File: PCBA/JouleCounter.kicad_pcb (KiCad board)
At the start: 2 copper layers, 5 x 8.2 mm, 31 parts, among them J501 USB_C_Receptacle, J502 USB_C_Receptacle_USB2.0, J601 USB_C_Receptacle_USB2.0, SW801 SW_Push, SW802 SW_Push, SW803 SW_Push, SW804 SW_Push, U201 BL604, U401 FUSB302B, U601 CH340E, U701 INA181

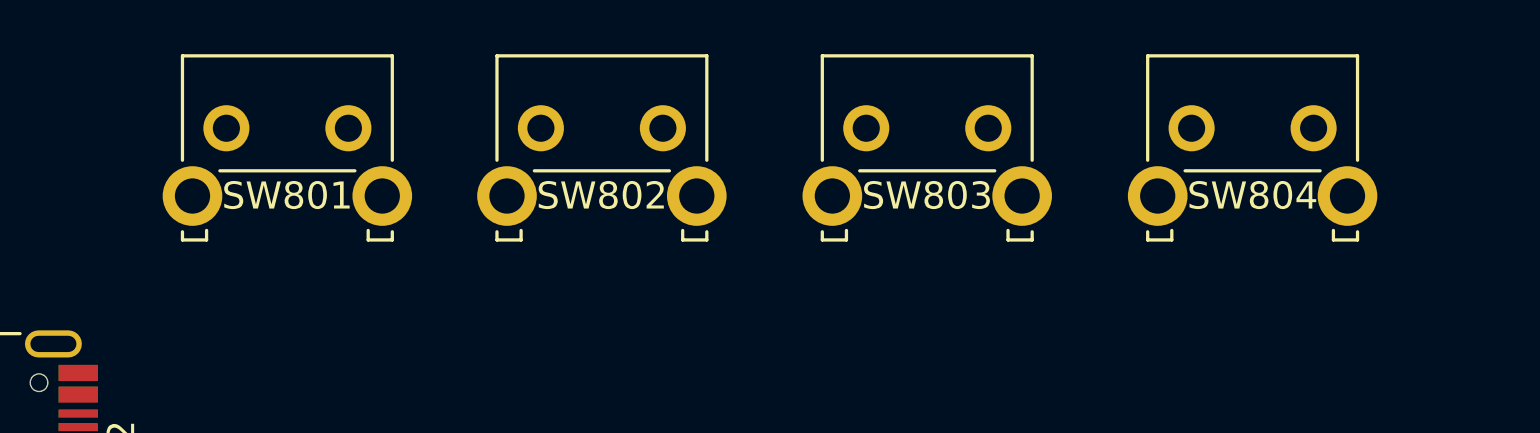
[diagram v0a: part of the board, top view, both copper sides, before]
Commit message: Assign footprints
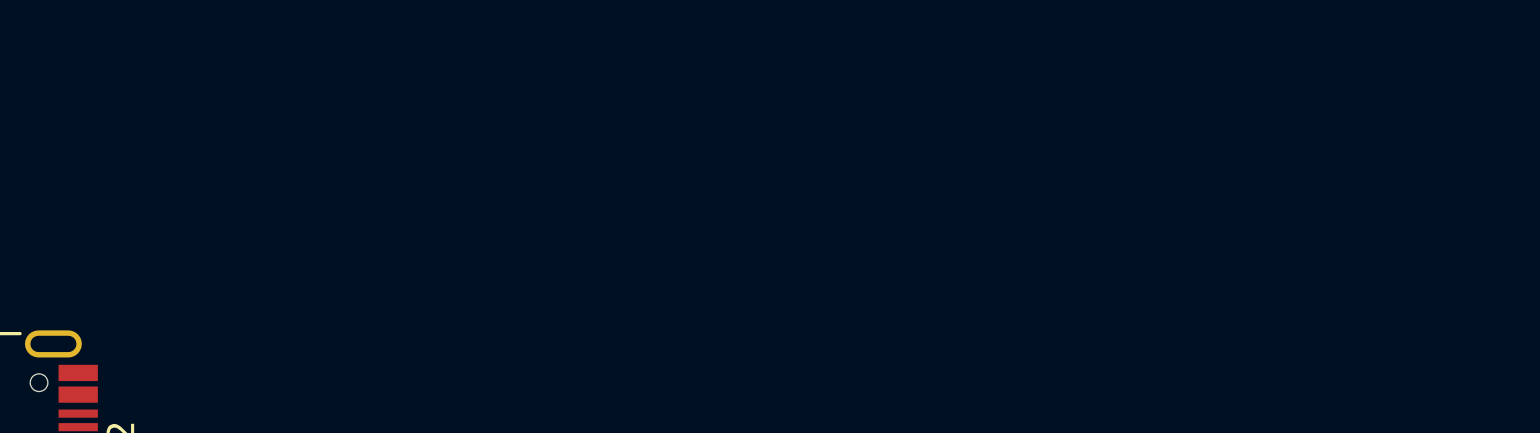
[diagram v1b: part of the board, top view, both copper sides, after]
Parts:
- removed SW801, SW802, SW803, SW804: SW_Push, Button_Switch_THT:SW_Tactile_SKHH_Angled

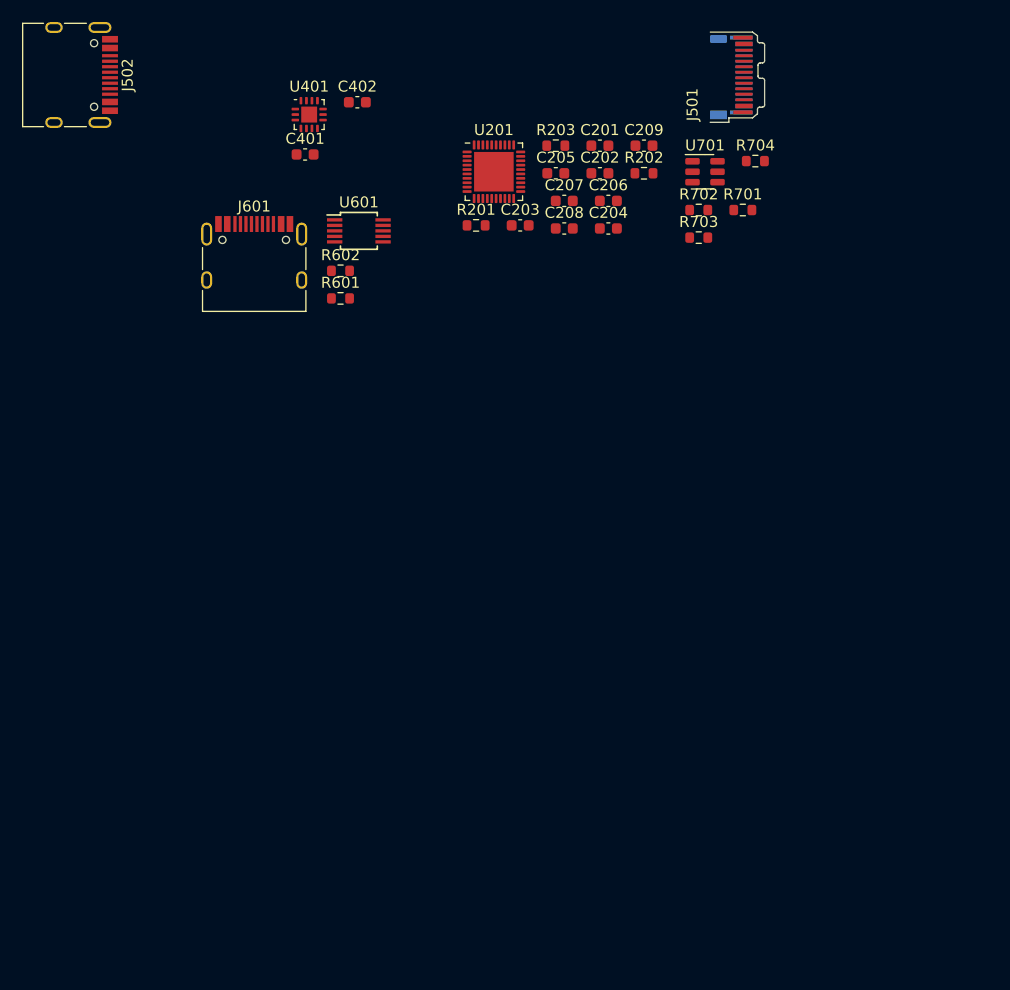
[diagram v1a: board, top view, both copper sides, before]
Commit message: Update schematic pinmap bl706
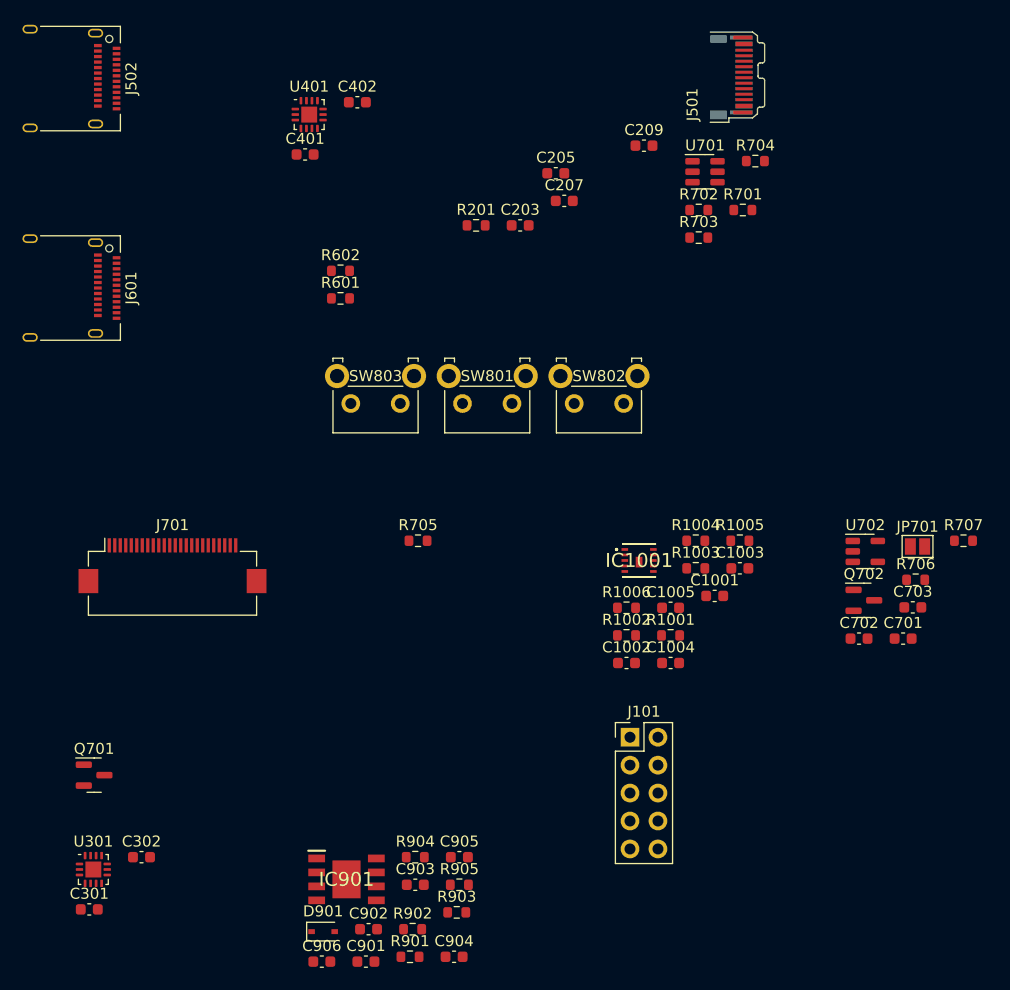
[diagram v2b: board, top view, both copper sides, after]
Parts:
- removed C201, C204: 0.1uF, Capacitor_SMD:C_0603_1608Metric
- removed C202, C206, C208: 1uF, Capacitor_SMD:C_0603_1608Metric
- removed R202, R203: 10k, Resistor_SMD:R_0603_1608Metric
- removed U201: BL604, Package_DFN_QFN:QFN-40-1EP_5x5mm_P0.4mm_EP3.6x3.6mm
- removed U601: CH340E, Package_SO:MSOP-10_3x3mm_P0.5mm
- added C1001: 100nF, Capacitor_SMD:C_0603_1608Metric, F.Cu at (158.5, 107.4)
- added C1002: 2.2uF, Capacitor_SMD:C_0603_1608Metric, F.Cu at (150.5, 113.5)
- added C1003: 2.2uF, Capacitor_SMD:C_0603_1608Metric, F.Cu at (160.8, 104.9)
- added C1004: 2.2uF, Capacitor_SMD:C_0603_1608Metric, F.Cu at (154.5, 113.5)
- added C1005: C, Capacitor_SMD:C_0603_1608Metric, F.Cu at (154.5, 108.5)
- added C301: 1uF, Capacitor_SMD:C_0603_1608Metric, F.Cu at (101.6, 135.9)
- added C302: 1uF, Capacitor_SMD:C_0603_1608Metric, F.Cu at (106.3, 131.1)
- added C701: C, Capacitor_SMD:C_0603_1608Metric, F.Cu at (175.6, 111.3)
- added C702: C, Capacitor_SMD:C_0603_1608Metric, F.Cu at (171.6, 111.3)
- added C703: C, Capacitor_SMD:C_0603_1608Metric, F.Cu at (176.5, 108.4)
- added C901: 47uF, Capacitor_SMD:C_0603_1608Metric, F.Cu at (126.8, 140.6)
- added C902: 4.7uF, Capacitor_SMD:C_0603_1608Metric, F.Cu at (127.0, 137.7)
- added C903: -, Capacitor_SMD:C_0603_1608Metric, F.Cu at (131.2, 133.7)
- added C904: -, Capacitor_SMD:C_0603_1608Metric, F.Cu at (134.8, 140.2)
- added C905: 100nF, Capacitor_SMD:C_0603_1608Metric, F.Cu at (135.3, 131.1)
- added C906: 4.7uF, Capacitor_SMD:C_0603_1608Metric, F.Cu at (122.8, 140.6)
- added D901: D_Schottky, Diode_SMD:D_SOD-323, F.Cu at (122.9, 137.9)
- added IC1001: L7983PU33R, L7983PU33R:L7983PU33R, F.Cu at (151.6, 104.2)
- added IC901: MP4560DN-LF-Z, MP4560DN:SOIC127P600X170-9N, F.Cu at (125.0, 133.2)
- added J101: JTAG, Connector_PinHeader_2.54mm:PinHeader_2x05_P2.54mm_Vertical, F.Cu at (150.8, 120.2)
- added J701: FH12-24S-0.5SH(55), Connector_FFC-FPC:Hirose_FH12-24S-0.5SH_1x24-1MP_P0.50mm_Horizontal, F.Cu at (109.2, 104.6)
- added JP701: Disable, Jumper:SolderJumper-2_P1.3mm_Open_Pad1.0x1.5mm, F.Cu at (176.9, 102.9)
- added Q701: 2N7002, Package_TO_SOT_SMD:SOT-23, F.Cu at (102.0, 123.7)
- added Q702: MMBT3904, Package_TO_SOT_SMD:SOT-23, F.Cu at (172.1, 107.8)
- added R1001: 0, Resistor_SMD:R_0603_1608Metric, F.Cu at (154.5, 111.0)
- added R1002: DNP, Resistor_SMD:R_0603_1608Metric, F.Cu at (150.5, 111.0)
- added R1003: 0, Resistor_SMD:R_0603_1608Metric, F.Cu at (156.8, 104.9)
- added R1004: 100k, Resistor_SMD:R_0603_1608Metric, F.Cu at (156.8, 102.4)
- added R1005: 180k, Resistor_SMD:R_0603_1608Metric, F.Cu at (160.8, 102.4)
- added R1006: 68k, Resistor_SMD:R_0603_1608Metric, F.Cu at (150.5, 108.5)
- added R705: 200?, Resistor_SMD:R_0603_1608Metric, F.Cu at (131.5, 102.4)
- added R706: 100k, Resistor_SMD:R_0603_1608Metric, F.Cu at (176.8, 105.9)
- added R707: 1M, Resistor_SMD:R_0603_1608Metric, F.Cu at (181.1, 102.4)
- added R901: 200k, Resistor_SMD:R_0603_1608Metric, F.Cu at (130.8, 140.2)
- added R902: -, Resistor_SMD:R_0603_1608Metric, F.Cu at (131.0, 137.7)
- added R903: -, Resistor_SMD:R_0603_1608Metric, F.Cu at (135.0, 136.2)
- added R904: 200k, Resistor_SMD:R_0603_1608Metric, F.Cu at (131.2, 131.1)
- added R905: 200k, Resistor_SMD:R_0603_1608Metric, F.Cu at (135.3, 133.7)
- added SW801: SW_Push, Button_Switch_THT:SW_Tactile_SKHH_Angled, F.Cu at (140.0, 89.9)
- added SW802: SW_Push, Button_Switch_THT:SW_Tactile_SKHH_Angled, F.Cu at (150.2, 89.9)
- added SW803: SW_Push, Button_Switch_THT:SW_Tactile_SKHH_Angled, F.Cu at (129.9, 89.9)
- added U301: FUSB302B, Package_DFN_QFN:WQFN-14-1EP_2.5x2.5mm_P0.5mm_EP1.45x1.45mm, F.Cu at (102.0, 132.3)
- added U702: TC2014-3.3VxCTTR, Package_TO_SOT_SMD:SOT-23-5, F.Cu at (172.2, 103.3)
- J502, J601: value USB_C_Receptacle_USB2.0 -> USB_C_Receptacle; footprint Connector_USB:USB_C_Receptacle_HRO_TYPE-C-31-M-12 -> Connector_USB:USB_C_Receptacle_Amphenol_12401610E4-2A
- moved J601 17.6 mm to (99.1, 79.4), turned to -90 degrees
- moved J502 0.50 mm to (99.1, 60.3)
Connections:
- net /Programming/5V renamed /5V_USB
- net /~{FUSB IRQ} renamed /~{FUSB IRQ0}
- net AVDD33 renamed VDD
- net Net-(J601-PadA6) renamed /USB D+
- net Net-(J601-PadA7) renamed /USB D-
- J501 pad A10: unconnected-(J501-PadA10) -> Net-(J501-PadA10)
- J501 pad A11: unconnected-(J501-PadA11) -> Net-(J501-PadA11)
- J501 pad A2: unconnected-(J501-PadA2) -> Net-(J501-PadA2)
- J501 pad A3: unconnected-(J501-PadA3) -> Net-(J501-PadA3)
- J501 pad B10: unconnected-(J501-PadB10) -> Net-(J501-PadB10)
- J501 pad B11: unconnected-(J501-PadB11) -> Net-(J501-PadB11)
- J501 pad B2: unconnected-(J501-PadB2) -> Net-(J501-PadB2)
- J501 pad B3: unconnected-(J501-PadB3) -> Net-(J501-PadB3)
- J502 pad A5: /CC1 -> /CC1_X
- J502 pad B5: /CC2 -> /CC2_X
- J601 pad A8: unconnected-(J601-PadA8) -> /Uart Tx
- J601 pad B8: unconnected-(J601-PadB8) -> /Uart Rx
- R201 pad 1: /BootMode -> unconnected-(R201-Pad1)

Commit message: Rough outline
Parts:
- removed J701: FH12-24S-0.5SH(55), Connector_FFC-FPC:Hirose_FH12-24S-0.5SH_1x24-1MP_P0.50mm_Horizontal
- removed R705: 200?, Resistor_SMD:R_0603_1608Metric
- added AE201: KH2012F245C04, Resistor_SMD:R_0805_2012Metric, F.Cu at (231.4, 123.0)
- added C201: 1uF, Capacitor_SMD:C_0603_1608Metric, F.Cu at (252.8, 116.6)
- added C202: 1uF, Capacitor_SMD:C_0603_1608Metric, F.Cu at (247.8, 119.2)
- added C204: 1uF, Capacitor_SMD:C_0603_1608Metric, F.Cu at (243.5, 122.4)
- added C206: 100nF, Capacitor_SMD:C_0603_1608Metric, F.Cu at (247.8, 121.7)
- added C208: 1uF, Capacitor_SMD:C_0603_1608Metric, F.Cu at (252.8, 114.1)
- added C210: 100nF, Capacitor_SMD:C_0603_1608Metric, F.Cu at (256.8, 114.1)
- added C211: -, Capacitor_SMD:C_0603_1608Metric, F.Cu at (251.8, 119.2)
- added C212: -, Capacitor_SMD:C_0603_1608Metric, F.Cu at (247.5, 124.2)
- added C213: 0.1uF, Capacitor_SMD:C_0603_1608Metric, F.Cu at (256.4, 117.8)
- added C907: C, Capacitor_SMD:C_0603_1608Metric, F.Cu at (178.6, 55.4)
- added C908: 0.1u, Capacitor_SMD:C_0603_1608Metric, F.Cu at (178.6, 60.4)
- added C909: 0.1u, Capacitor_SMD:C_0603_1608Metric, F.Cu at (178.6, 57.9)
- added C910: 0.1u, Capacitor_SMD:C_0603_1608Metric, F.Cu at (182.6, 57.9)
- added C911: 1uf, Capacitor_SMD:C_0603_1608Metric, F.Cu at (182.6, 55.4)
- added J901: Conn_02x25_Odd_Even_MountingPin, Connector_FFC-FPC:Molex_54132-5033_1x50-1MP_P0.5mm_Horizontal, F.Cu at (215.4, 81.9)
- added L1001: 47uH, Inductor_SMD:L_Taiyo-Yuden_NR-40xx_HandSoldering, F.Cu at (179.8, 21.2)
- added L201: 2.2uH, Inductor_SMD:L_Wuerth_MAPI-3010, F.Cu at (248.3, 115.4)
- added L901: 15, Inductor_SMD:L_Wuerth_MAPI-3010, F.Cu at (162.2, 35.2)
- added R202: 0, Resistor_SMD:R_0603_1608Metric, F.Cu at (239.5, 122.4)
- added R501: 0.02, Resistor_SMD:R_Shunt_Vishay_WSK2512_6332Metric_T1.19mm, F.Cu at (230.5, 92.1)
- added R906: 200?, Resistor_SMD:R_0603_1608Metric, F.Cu at (183.5, 46.5)
- added R907: 200?, Resistor_SMD:R_0603_1608Metric, F.Cu at (178.4, 50.9)
- added R908: 200?, Resistor_SMD:R_0603_1608Metric, F.Cu at (186.4, 49.0)
- added R909: 200?, Resistor_SMD:R_0603_1608Metric, F.Cu at (182.4, 50.9)
- added SW501: SW_DIP_x02, Button_Switch_SMD:SW_DIP_SPSTx02_Slide_Copal_CHS-02A_W5.08mm_P1.27mm_JPin, B.Cu at (230.4, 67.8)
- added U201: BL706, Package_DFN_QFN:QFN-48-1EP_6x6mm_P0.4mm_EP4.2x4.2mm, F.Cu at (213.0, 94.3)
- added U901: LP2985-2.8, Package_TO_SOT_SMD:SOT-23-5, F.Cu at (178.9, 47.5)
- added Y201: 40MHz, Crystal:Crystal_SMD_2016-4Pin_2.0x1.6mm, F.Cu at (251.7, 122.2)
- moved J502 138.8 mm to (230.5, 104.8), turned to 0 degrees
- moved Q701 134.1 mm to (213.2, 48.6)
- moved C203 129.1 mm to (257.4, 129.1)
- moved C205 129.1 mm to (260.6, 124.4)
- moved C207 129.1 mm to (261.4, 126.9)
- moved C209 129.1 mm to (268.6, 121.9)
- moved R201 129.1 mm to (253.3, 129.1)
- moved C301 125.6 mm to (222.5, 101.8)
- moved U301 123.7 mm to (222.5, 104.5), turned to -90 degrees
- moved C302 118.6 mm to (222.5, 107.2), turned to 180 degrees
- moved C903 114.7 mm to (162.5, 23.3)
- moved R905 114.7 mm to (166.5, 23.3)
- moved C902 114.7 mm to (158.2, 27.3)
- moved R902 114.7 mm to (162.2, 27.3)
- moved C901 114.7 mm to (158.0, 30.3)
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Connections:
- net /USB D+ DAC/ADC renamed /SENSE_USB_D+
- net /USB D- DAC/ADC renamed /SENSE_USB_D-
- net Net-(J501-PadA10) renamed /Measurement ports/RX2_-
- net Net-(J501-PadA11) renamed /Measurement ports/RX2_+
- net Net-(J501-PadA2) renamed /Measurement ports/TX1_+
- net Net-(J501-PadA3) renamed /Measurement ports/TX1_-
- net Net-(J501-PadA4) renamed /Measurement ports/VBUS2
- net Net-(J501-PadA8) renamed /Measurement ports/SBU1
- net Net-(J501-PadB10) renamed /Measurement ports/RX1_-
- net Net-(J501-PadB11) renamed /Measurement ports/RX1_+
- net Net-(J501-PadB2) renamed /Measurement ports/TX2_+
- net Net-(J501-PadB3) renamed /Measurement ports/TX2_-
- net Net-(J501-PadB8) renamed /Measurement ports/SBU2
- Q701 pad 3: Net-(J701-Pad2) -> /UI/LEDK
- R201 pad 1: unconnected-(R201-Pad1) -> /~{Reset}
- R201 pad 2: GND -> VDD
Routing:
- net /Measurement ports/RX1_+: track 0.00 -> 48.5 mm, vias 0 -> 1
- net /Measurement ports/RX1_-: track 0.00 -> 48.5 mm, vias 0 -> 1
- net /Measurement ports/TX2_-: track 0.00 -> 47.1 mm, vias 0 -> 1
- net /Measurement ports/TX2_+: track 0.00 -> 47.1 mm, vias 0 -> 1
- net /Measurement ports/TX1_+: track 0.00 -> 43.6 mm
- net /Measurement ports/TX1_-: track 0.00 -> 43.6 mm
- net /SENSE_USB_D-: track 0.00 -> 43.6 mm
- net /SENSE_USB_D+: track 0.00 -> 43.6 mm
- net /Measurement ports/RX2_+: track 0.00 -> 41.9 mm
- net /Measurement ports/RX2_-: track 0.00 -> 41.9 mm
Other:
- board size 5 x 8.2 mm -> 42 x 49 mm
- copper layers 2 -> 4

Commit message: More rough placement
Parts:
- L201: footprint Inductor_SMD:L_Wuerth_MAPI-3010 -> Inductor_SMD:L_0805_2012Metric
- moved C209 66.8 mm to (210.2, 89.5)
- moved U702 60.1 mm to (207.5, 104.5), turned to 90 degrees
- moved C205 57.2 mm to (215.5, 89.2)
- moved C201 51.7 mm to (206.0, 94.8), turned to 180 degrees
- moved C213 50.4 mm to (209.0, 100.8), turned to 180 degrees
- moved C202 47.6 mm to (206.0, 96.2), turned to 180 degrees
- moved Y201 45.2 mm to (219.5, 90.5)
- moved C203 44.5 mm to (213.0, 125.0)
- moved C207 44.5 mm to (217.0, 122.8)
- moved R201 44.5 mm to (209.0, 125.0)
- moved C211 43.1 mm to (211.8, 103.0), turned to 180 degrees
- moved L201 42.5 mm to (209.0, 99.0)
- moved C212 40.6 mm to (211.8, 104.8), turned to 180 degrees
- moved C210 40.4 mm to (221.2, 95.0)
- moved C701 38.6 mm to (177.6, 77.0)
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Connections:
- C204 pad 2: Net-(C204-Pad2) -> GND
- C206 pad 2: Net-(C204-Pad2) -> GND
- C208 pad 2: Net-(C204-Pad2) -> GND
- C210 pad 2: Net-(C204-Pad2) -> GND
- U201 pad 18: /SENSE_USB_D- -> /SENSE_USB_D+
- U201 pad 32: /USB D- DAC/ADC -> /SENSE_USB_D-
- U201 pad 33: /USB D- DAC/ADC -> /SENSE_USB_D-
- U201 pad 34: /Current ADC -> /VBus ADC
- U201 pad 35: /VBus ADC -> /Current ADC
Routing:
- net GND: track 0.00 -> 20.9 mm, vias 0 -> 2
- net /VBus ADC: track 0.00 -> 11.1 mm
- net /I Sense 1: track 0.00 -> 9.37 mm, vias 0 -> 2
- net /Current ADC: track 0.00 -> 8.11 mm
- net /I Sense 2: track 0.00 -> 5.82 mm, vias 0 -> 2
- net /VBus: track 0.00 -> 5.70 mm, vias 0 -> 2
- net VDD: track 0.00 -> 5.27 mm
- net /CC1_X: track 0.00 -> 4.35 mm
- net /ADC Measurements/VRef: track 0.00 -> 4.19 mm
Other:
- board text added: "1"

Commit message: Routing
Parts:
- removed C910: 0.1u, Capacitor_SMD:C_0603_1608Metric
- L1001: footprint Inductor_SMD:L_Taiyo-Yuden_NR-40xx_HandSoldering -> Inductor_SMD:L_1210_3225Metric
- moved R904 70.8 mm to (219.5, 62.8), turned to 180 degrees
- moved IC901 68.4 mm to (205.5, 70.2)
- moved C906 67.8 mm to (210.0, 68.5), turned to -90 degrees
- moved R905 65.0 mm to (210.0, 71.5), turned to -90 degrees
- moved C902 64.2 mm to (209.2, 66.2), turned to 180 degrees
- moved C901 61.8 mm to (209.2, 64.8), turned to 180 degrees
- moved C903 61.4 mm to (200.5, 71.5), turned to 90 degrees
- moved D901 61.4 mm to (202.5, 65.2), turned to 90 degrees
- moved C905 60.1 mm to (205.5, 66.5)
- moved R902 58.3 mm to (209.2, 61.8)
- moved R901 57.9 mm to (209.2, 63.2), turned to 180 degrees
- moved R1003 56.4 mm to (218.8, 73.8), turned to -90 degrees
- moved R1004 56.0 mm to (221.2, 68.8), turned to 90 degrees
- moved IC1001 55.8 mm to (217.8, 68.8), turned to 90 degrees
- moved L1001 55.7 mm to (215.5, 64.0), turned to 180 degrees
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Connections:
- net Net-(AE201-Pad2) renamed /Main MCU/ANT
- net Net-(C211-Pad1) renamed /Main MCU/RF
- J601 pad A10: /SDA -> /Spare GPIO 0
- J601 pad A11: /SCL -> /Spare GPIO 1
- J601 pad A2: /Spare GPIO 1 -> /SCL
- J601 pad A3: /Spare GPIO 0 -> /SDA
- SW801 pad 1: /Button A -> /BootMode
- SW802 pad 1: /BootMode -> /Button C
- SW803 pad 1: /Button C -> /Button A
- U201 pad 37: /Spare GPIO 1 -> /LCD DC
- U201 pad 42: /LCD DC -> /~{TOUCH_IRQ}
- U201 pad 46: /~{TOUCH_IRQ} -> /Spare GPIO 1
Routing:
- net GND: track 20.9 -> 100.8 mm, vias 2 -> 20
- net VDD: track 5.27 -> 71.5 mm, vias 0 -> 5
- net /Button A: track 0.00 -> 34.1 mm, vias 0 -> 1
- net /SENSE_USB_D+: track 43.6 -> 71.9 mm, vias 0 -> 2
- net /SENSE_USB_D-: track 43.6 -> 70.4 mm, vias 0 -> 3
- net /Button C: track 0.00 -> 25.2 mm, vias 0 -> 1
- net /BootMode: track 0.00 -> 23.8 mm, vias 0 -> 1
- net /~{Reset}: track 0.00 -> 23.7 mm, vias 0 -> 2
- net /UI/VDD2.8: track 0.00 -> 23.1 mm
- net /~{TOUCH_IRQ}: track 0.00 -> 22.1 mm, vias 0 -> 2
- net /~{FUSB IRQ1}: track 0.00 -> 21.3 mm, vias 0 -> 2
- net /LCD PWM: track 0.00 -> 19.6 mm, vias 0 -> 2
- net /SCL: track 0.00 -> 19.6 mm, vias 0 -> 2
- net /USB D-: track 0.00 -> 18.6 mm, vias 0 -> 2
- net /Uart Rx: track 0.00 -> 18.5 mm, vias 0 -> 2
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- added copper zone on B.Cu, net GND
